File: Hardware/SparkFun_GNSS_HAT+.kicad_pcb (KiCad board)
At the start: 4 copper layers, 65 x 56.8 mm, 81 parts, among them J1 Raspberry_Pi_2x20_SMD_Passthr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, J2 Conn_02x10, J3 U.FL, J4 Conn_02x10, J5 microSD, J6 USB_C_Receptacle, J7 SMA_Edge, J8 Qwiic_RA, U1 CAT24C512WI-GT3, U2 AP7361C-3.3V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

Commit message: More WIP
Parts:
- removed the G*** at (225.9, 70.3)
- added G***: LOGO, SparkFun-Aesthetic:qwiic_6mm, F.Cu at (174.8, 90.7)
- added G***: LOGO, SparkFun-Aesthetic:SparkPNT_Logo_20mm, F.Cu at (160.6, 90.9)
- added ST1: Standoff, SparkFun-Hardware:Standoff, F.Cu at (127.1, 82.0)
- added ST2: Standoff, SparkFun-Hardware:Standoff, F.Cu at (156.1, 82.0)
- added ST3: Standoff, SparkFun-Hardware:Standoff, F.Cu at (156.1, 121.0)
- added ST4: Standoff, SparkFun-Hardware:Standoff, F.Cu at (127.1, 121.0)
- added kibuzzard-678A80FB: G***, kibuzzard-678A80FB, F.Cu at (178.2, 101.6)
- added kibuzzard-678A8134: G***, kibuzzard-678A8134, F.Cu at (178.1, 99.1)
- added kibuzzard-678A8173: G***, kibuzzard-678A8173, F.Cu at (178.1, 96.5)
- J5: value microSD -> microSD_Friction; footprint SparkFun-Connector:microSD_External_Pin -> SparkFun-Connector:microSD_Friction_Fit_Common
- J8: value Qwiic_RA -> Qwiic_Vertical; footprint SparkFun-Connector:JST_SMD_1.0mm-4_RA -> SparkFun-Connector:JST_SMD_1.0mm-4_Vertical
- JP10, JP11, JP12, JP15, JP16, JP17, JP19, JP20, JP21, JP6: value Measure -> ~; footprint SparkFun-Jumper:Jumper_2_PTH_SMD_Combo-NC -> SparkFun-Jumper:Jumper_2_NC_Trace
- JP13, JP14, JP18, JP4, JP5, JP7: value Measure -> ~; footprint SparkFun-Jumper:Jumper_2_PTH_SMD_Combo-NC -> SparkFun-Jumper:Jumper_2_NC_Trace; moved to B.Cu
- JP3, JP8, JP9: moved to B.Cu
- moved JP3 147.9 mm to (118.1, 80.5), turned to 180 degrees
- moved C5 129.8 mm to (138.5, 110.5), turned to -90 degrees
- moved U2 127.0 mm to (141.6, 92.5)
- moved C4 125.4 mm to (144.6, 110.5), turned to 90 degrees
- moved R10 125.4 mm to (126.1, 85.6), turned to 180 degrees
- moved C3 124.8 mm to (138.5, 92.5), turned to 90 degrees
- moved R9 123.8 mm to (126.1, 78.4), turned to 180 degrees
- moved JP8 121.7 mm to (144.3, 77.5), turned to 90 degrees
- moved JP4 121.0 mm to (131.6, 77.5), turned to 90 degrees
- moved TR1 120.1 mm to (129.3, 96.5), turned to -90 degrees
- moved C2 120.0 mm to (144.6, 92.5), turned to 90 degrees
- moved JP5 117.3 mm to (134.1, 77.5), turned to 90 degrees
- moved D1 116.5 mm to (126.2, 91.4), turned to -90 degrees
- moved JP9 115.7 mm to (149.4, 77.5), turned to 90 degrees
- moved JP10 115.5 mm to (131.6, 77.5), turned to -90 degrees
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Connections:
- JP10 pad 1: RXD1 -> Net-(J1-GCLK0/GPIO4)
- JP10 pad 2: Net-(J1-GPIO14/TXD) -> RXD3
- JP11 pad 1: TXD1 -> Net-(J1-GCLK1/GPIO5)
- JP11 pad 2: Net-(J1-GPIO15/RXD) -> TXD3
- JP12 pad 1: RXD3 -> Net-(J1-GCLK2/GPIO6)
- JP12 pad 2: Net-(J1-GCLK0/GPIO4) -> RTS3
- JP13 pad 1: TXD3 -> Net-(J1-~{CE1}/GPIO7)
- JP13 pad 2: Net-(J1-GCLK1/GPIO5) -> CTS3
- JP14 pad 1: RXD2 -> Net-(J1-~{CE0}/GPIO8)
- JP14 pad 2: Net-(J1-~{CE0}/GPIO8) -> RXD2
- JP15 pad 1: TXD2 -> Net-(J1-POCI0/GPIO9)
- JP15 pad 2: Net-(J1-POCI0/GPIO9) -> TXD2
- JP16 pad 1: RXD4 -> Net-(J1-PICO0/GPIO10)
- JP16 pad 2: Net-(J1-PWM0/GPIO12) -> RTS2
- JP17 pad 1: TXD4 -> Net-(J1-SCLK0/GPIO11)
- JP17 pad 2: Net-(J1-PWM1/GPIO13) -> CTS2
- JP18 pad 1: RTS3 -> Net-(J1-PWM0/GPIO12)
- JP18 pad 2: Net-(J1-GCLK2/GPIO6) -> RXD4
- JP19 pad 1: CTS3 -> Net-(J1-PWM1/GPIO13)
- JP19 pad 2: Net-(J1-~{CE1}/GPIO7) -> TXD4
- JP20 pad 1: RTS2 -> RTK_LED
- JP20 pad 2: Net-(J1-PICO0/GPIO10) -> Net-(JP20-B)
- JP21 pad 1: CTS2 -> PVT_LED
- JP21 pad 2: Net-(J1-SCLK0/GPIO11) -> Net-(JP21-B)
- JP22 pad 1: Net-(JP22-A) -> PPS1
- JP22 pad 2: PPS1 -> Net-(JP22-B)
- JP4 pad 1: PPS1 -> RXD1
- JP4 pad 2: Net-(J1-GPIO22) -> Net-(J1-GPIO14/TXD)
- JP5 pad 1: PPS2 -> TXD1
- JP5 pad 2: Net-(J1-GPIO23) -> Net-(J1-GPIO15/RXD)
- JP6 pad 1: EVENTA -> PPS1
- JP6 pad 2: Net-(J1-GPIO24) -> Net-(J1-GPIO22)
- JP7 pad 1: EVENTB -> PPS2
- JP7 pad 2: Net-(J1-GPIO25) -> Net-(J1-GPIO23)
- JP8 pad 1: Net-(JP8-A) -> EVENTA
- JP8 pad 2: RTK_LED -> Net-(J1-GPIO24)
- JP9 pad 1: Net-(JP9-A) -> EVENTB
- JP9 pad 2: PVT_LED -> Net-(J1-GPIO25)
- R11 pad 2: Net-(JP8-A) -> Net-(JP20-B)
- R12 pad 2: Net-(JP9-A) -> Net-(JP21-B)
- R13 pad 2: Net-(JP22-A) -> Net-(JP22-B)
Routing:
- net 3.3V: track 0.00 -> 6.17 mm, vias 0 -> 1
- net GND: vias 0 -> 19
- added copper zone on In2.Cu, net 3.3V
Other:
- board text added: "1"
- board text added: "2"
- board text added: "3"
- board text added: "4"

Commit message: More WIP
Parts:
- removed H1, H2, H3, H4: MountingHole, MountingHole:MountingHole_2.7mm_M2.5_DIN965
- added ST5: Standoff, SparkFun-Hardware:Standoff_Raspberry-Pi_HAT+, F.Cu at (119.1, 72.0)
- added ST6: Standoff, SparkFun-Hardware:Standoff_Raspberry-Pi_HAT+, F.Cu at (119.1, 121.0)
- added ST7: Standoff, SparkFun-Hardware:Standoff_Raspberry-Pi_HAT+, F.Cu at (177.1, 121.0)
- added ST8: Standoff, SparkFun-Hardware:Standoff_Raspberry-Pi_HAT+, F.Cu at (177.1, 72.0)
- moved TR1 3.05 mm to (126.2, 96.6)
- turned D1 to 90 degrees
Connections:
- TR1 pad 1: Net-(D1-I/O1) -> Net-(D1-I/O2)
- TR1 pad 2: D+ -> D-
- TR1 pad 3: Net-(D1-I/O2) -> Net-(D1-I/O1)
- TR1 pad 4: D- -> D+
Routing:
- net D+: track 0.00 -> 44.2 mm, vias 0 -> 2
- net D-: track 0.00 -> 43.7 mm, vias 0 -> 2
- net Net-(D1-I/O2): track 0.00 -> 21.7 mm
- net Net-(D1-I/O1): track 0.00 -> 20.1 mm
- net VUSB: track 0.00 -> 16.2 mm, vias 0 -> 3
- net GND: track 0.00 -> 6.62 mm, vias 19 -> 59
- net Net-(J6-CC2): track 0.00 -> 5.53 mm, vias 0 -> 2
- net Net-(J6-SHIELD): track 0.00 -> 4.47 mm
- net Net-(J6-CC1): track 0.00 -> 3.81 mm
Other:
- board text added: "v01"
- board text removed: "v10"

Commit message: Routed
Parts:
- added G***: LOGO, SparkFun-Aesthetic:SparkPNT_Logo_20mm, B.Cu at (148.1, 97.0)
- moved D2 9.00 mm to (166.8, 104.0), turned to 90 degrees
- moved C4 3.66 mm to (144.8, 106.8)
- moved C5 3.65 mm to (138.4, 106.8)
- moved U3 3.65 mm to (141.6, 106.8)
- moved R8 0.51 mm to (163.2, 107.7)
- moved R6 0.38 mm to (171.7, 107.7)
- moved C2 0.16 mm to (144.8, 92.5)
- moved C3 0.09 mm to (138.4, 92.5)
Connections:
- D2 pad 1: SD_DAT3 -> SD_DAT0
- D2 pad 3: SD_DAT0 -> SD_CLK
- D2 pad 4: SD_CLK -> SD_CMD
- D2 pad 5: SD_CMD -> SD_DAT3
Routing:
- net SDA: track 0.00 -> 103.0 mm, vias 0 -> 4
- net SCL: track 0.00 -> 102.7 mm, vias 0 -> 4
- net 5V: track 0.00 -> 97.2 mm, vias 0 -> 6
- net PPS1: track 0.00 -> 82.3 mm, vias 0 -> 5
- net Pi_3V3: track 0.00 -> 63.7 mm, vias 0 -> 4
- net SD_CMD: track 0.00 -> 56.0 mm, vias 0 -> 5
- net VUSB: track 16.2 -> 71.7 mm, vias 3 -> 5
- net EVENTA: track 0.00 -> 53.0 mm, vias 0 -> 3
- net SD_DAT3: track 0.00 -> 52.5 mm, vias 0 -> 3
- net SD_CLK: track 0.00 -> 49.6 mm, vias 0 -> 5
- net EVENTB: track 0.00 -> 48.3 mm, vias 0 -> 4
- net 3.3V: track 6.17 -> 53.8 mm, vias 1 -> 14
- net PPS2: track 0.00 -> 46.4 mm, vias 0 -> 3
- net SD_DAT0: track 0.00 -> 45.7 mm
- net RTK_LED: track 0.00 -> 45.5 mm
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
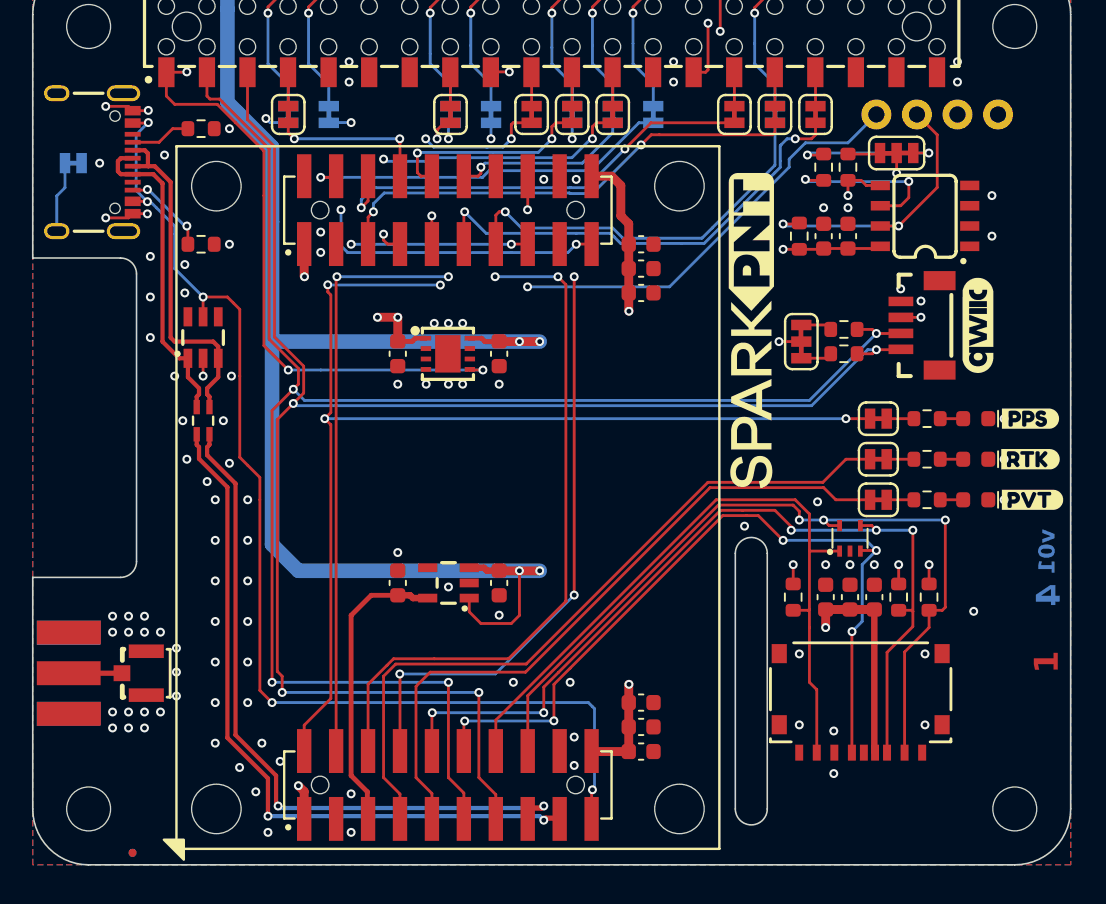
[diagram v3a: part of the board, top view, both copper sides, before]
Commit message: Panelized
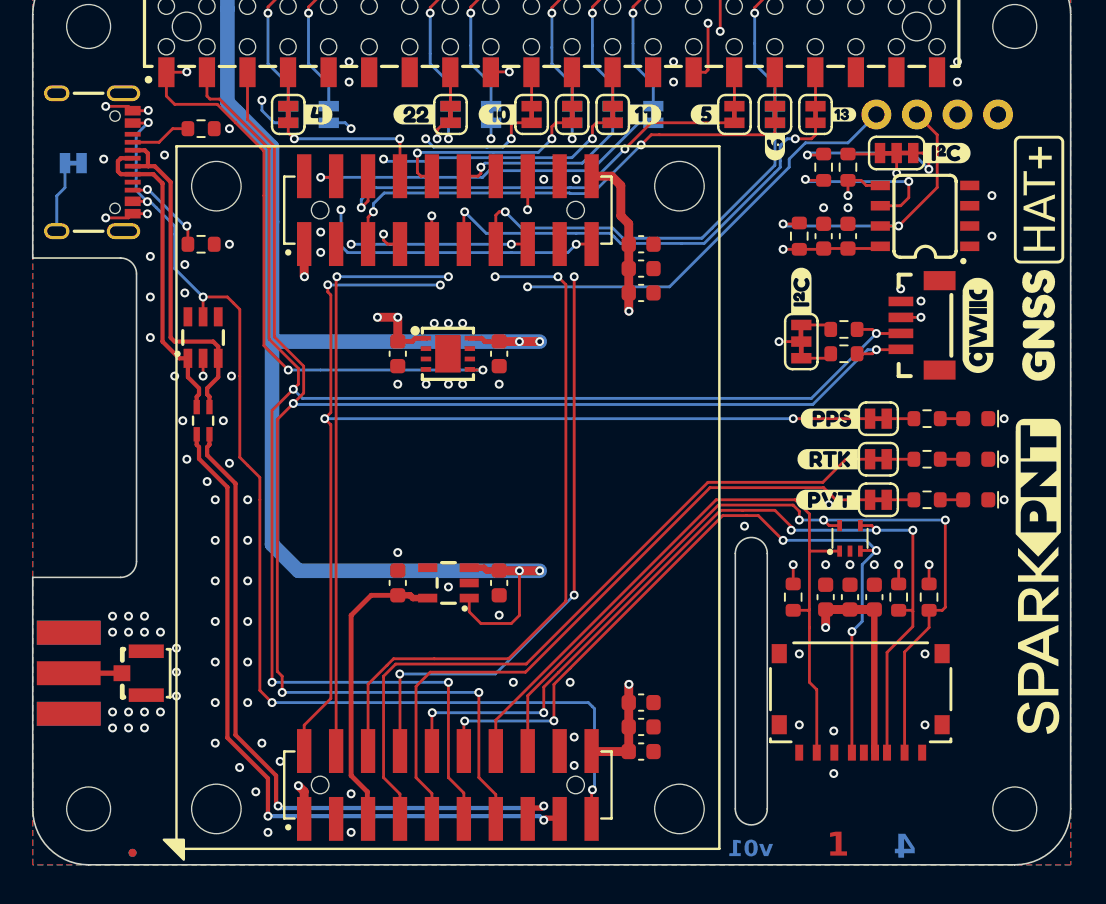
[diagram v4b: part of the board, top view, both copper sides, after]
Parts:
- removed kibuzzard-678A80FB: G***, kibuzzard-678A80FB
- removed kibuzzard-678A8134: G***, kibuzzard-678A8134
- removed kibuzzard-678A8173: G***, kibuzzard-678A8173
- added REF**: RPi_HAT+_8mm, SparkFun-Aesthetic:RPi_HAT+_8mm, F.Cu at (178.6, 82.8)
- added REF**: RPi_HAT+_8mm, SparkFun-Aesthetic:RPi_HAT+_8mm, B.Cu at (144.0, 100.5)
- added kibuzzard-678F852F: G***, kibuzzard-678F852F, F.Cu at (178.6, 90.7)
- added kibuzzard-678F852F: G***, kibuzzard-678F852F, B.Cu at (152.1, 100.5)
- added kibuzzard-678F8755: G***, kibuzzard-678F8755, F.Cu at (165.5, 96.5)
- added kibuzzard-678F8777: G***, kibuzzard-678F8777, F.Cu at (165.4, 99.1)
- added kibuzzard-678F878F: G***, kibuzzard-678F878F, F.Cu at (165.4, 101.6)
- added kibuzzard-678F893B: G***, kibuzzard-678F893B, F.Cu at (163.7, 88.5)
- added kibuzzard-678F893B: G***, kibuzzard-678F893B, F.Cu at (172.8, 79.9)
- added kibuzzard-678F89CB: G***, kibuzzard-678F89CB, B.Cu at (176.0, 79.9)
- added kibuzzard-678F89E9: G***, kibuzzard-678F89E9, B.Cu at (173.5, 79.8)
- added kibuzzard-678F8AD2: G***, kibuzzard-678F8AD2, B.Cu at (168.4, 80.0)
- added kibuzzard-678F8D59: G***, kibuzzard-678F8D59, F.Cu at (133.5, 77.5)
- added kibuzzard-678F8D86: G***, kibuzzard-678F8D86, F.Cu at (139.4, 77.5)
- added kibuzzard-678F8DB2: G***, kibuzzard-678F8DB2, F.Cu at (153.9, 77.5)
- added kibuzzard-678F8DFF: G***, kibuzzard-678F8DFF, F.Cu at (166.4, 77.5)
- added kibuzzard-678F8E11: G***, kibuzzard-678F8E11, F.Cu at (157.6, 77.5)
- added kibuzzard-678F8E25: G***, kibuzzard-678F8E25, F.Cu at (162.1, 79.5)
- added kibuzzard-678F8E41: G***, kibuzzard-678F8E41, F.Cu at (144.7, 77.5)
- added kibuzzard-678F8E95: G***, kibuzzard-678F8E95, B.Cu at (159.9, 77.5)
- added kibuzzard-678F8EB4: G***, kibuzzard-678F8EB4, B.Cu at (156.3, 77.5)
- added kibuzzard-678F8ED3: G***, kibuzzard-678F8ED3, B.Cu at (147.4, 77.0)
- added kibuzzard-678F8EED: G***, kibuzzard-678F8EED, B.Cu at (146.2, 78.0)
- added kibuzzard-678F8F11: G***, kibuzzard-678F8F11, B.Cu at (139.4, 77.5)
- added kibuzzard-678F8F2B: G***, kibuzzard-678F8F2B, B.Cu at (136.3, 77.5)
- added kibuzzard-678F8F42: G***, kibuzzard-678F8F42, B.Cu at (129.4, 77.5)
- added kibuzzard-678F8FC6: G***, kibuzzard-678F8FC6, B.Cu at (151.9, 79.2)
- added kibuzzard-678F918F: G***, kibuzzard-678F918F, B.Cu at (170.9, 79.8)
- added kibuzzard-678F92B8: G***, kibuzzard-678F92B8, B.Cu at (120.0, 80.5)
- moved G*** 23.7 mm to (178.6, 106.3)
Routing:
- net RXD1: track 30.1 -> 32.0 mm
- net Net-(JP2-A): track 9.68 -> 10.9 mm
- net GND: vias 114 -> 113
